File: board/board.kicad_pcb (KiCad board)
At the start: 2 copper layers, 21 x 29 mm, 12 parts, among them J1 004_BASE-T_CT_2x3, J2 013_PoE_rectified, Q1 TPN3300ANH,LQ, Q2 TPN3300ANH,LQ, Q3 TPN3300ANH,LQ, Q4 TPN3300ANH,LQ, Q5 TPN3300ANH,LQ, Q6 TPN3300ANH,LQ, Q7 TPN3300ANH,LQ, Q8 TPN3300ANH,LQ, U1 LT4321

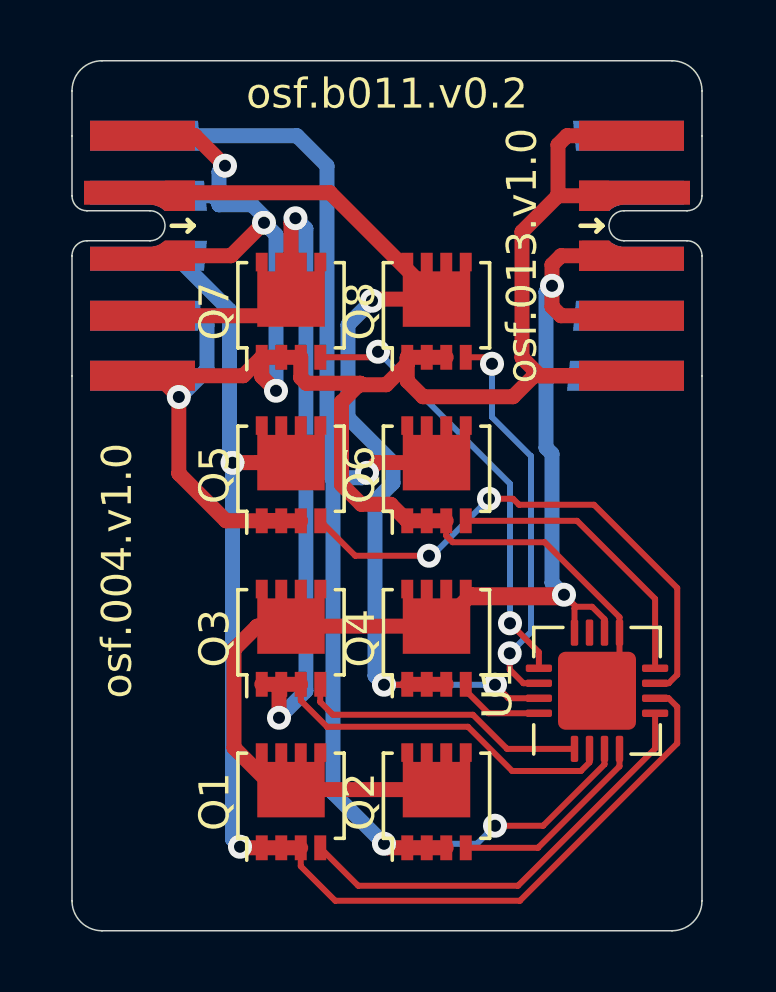
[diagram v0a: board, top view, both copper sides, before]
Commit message: updated connectors, changed mosfets and added enable resistors
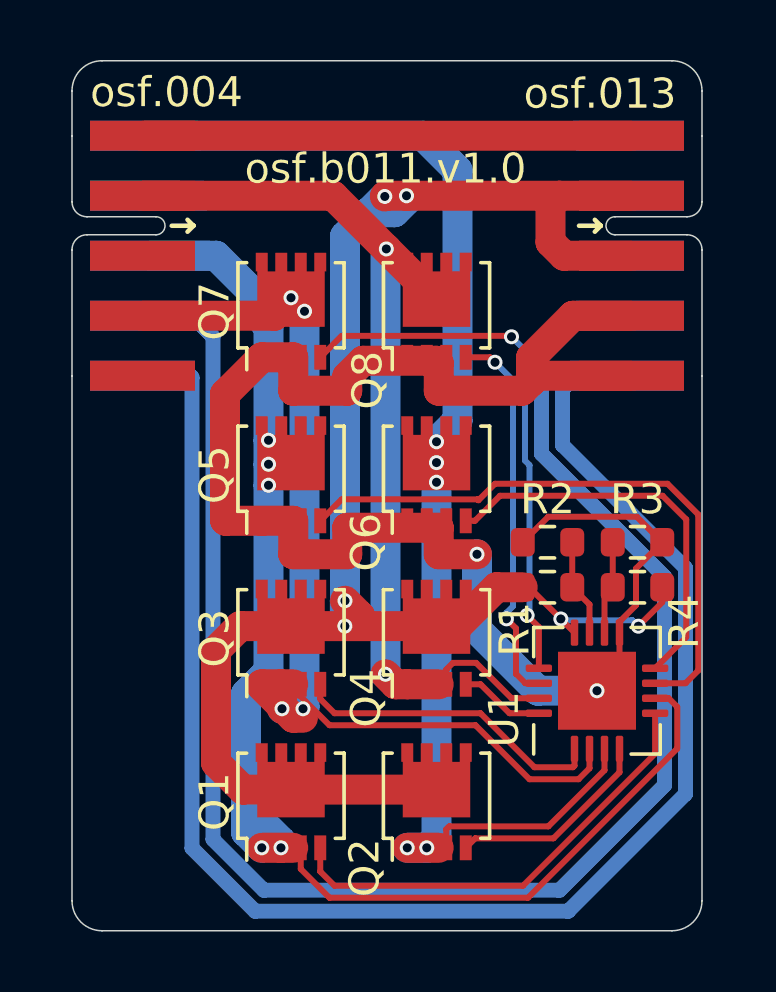
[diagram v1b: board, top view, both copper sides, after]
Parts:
- added R1: 0R, Resistor_SMD:R_0603_1608Metric, F.Cu at (135.8, 97.5)
- added R2: d.n.p, Resistor_SMD:R_0603_1608Metric, F.Cu at (135.8, 96.0)
- added R3: 0R, Resistor_SMD:R_0603_1608Metric, F.Cu at (138.8, 96.0)
- added R4: d.n.p, Resistor_SMD:R_0603_1608Metric, F.Cu at (138.8, 97.5)
- Q1, Q2, Q3, Q4, Q5, Q6, Q7, Q8: value TPN3300ANH,LQ -> PSMN075-100MSEX
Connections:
- J1 pad 10: GND -> Net-(J1-Pad10)
- J1 pad 3: GND -> (no net)
- J1 pad 5: GND -> (no net)
- J1 pad 7: GND -> (no net)
- J1 pad 9: GND -> Net-(J1-Pad9)
- J2 pad 10: (no net) -> Net-(J1-Pad10)
- J2 pad 2: GND -> /snippet/VPORTP
- J2 pad 4: /snippet/VPORTP -> /snippet/VPORTN
- J2 pad 5: GND -> /snippet/VPORTN
- J2 pad 9: (no net) -> Net-(J1-Pad9)
- Q5 pad 1: GND -> /snippet/VPORTN
- Q5 pad 2: GND -> /snippet/VPORTN
- Q5 pad 3: GND -> /snippet/VPORTN
- Q6 pad 1: GND -> /snippet/VPORTN
- Q6 pad 2: GND -> /snippet/VPORTN
- Q6 pad 3: GND -> /snippet/VPORTN
- Q7 pad 1: GND -> /snippet/VPORTN
- Q7 pad 2: GND -> /snippet/VPORTN
- Q7 pad 3: GND -> /snippet/VPORTN
- Q8 pad 1: GND -> /snippet/VPORTN
- Q8 pad 2: GND -> /snippet/VPORTN
- Q8 pad 3: GND -> /snippet/VPORTN
- U1 pad 10: /snippet/VPORTP -> /snippet/~{EN}
- U1 pad 11: /snippet/PWRGD -> /snippet/EN
- U1 pad 17: GND -> /snippet/VPORTN
- U1 pad 9: GND -> /snippet/VPORTN
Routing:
- net GND: track 90.0 -> 16.3 mm, vias 4 -> 0
- net Net-(J1-Pad9): track 0.00 -> 56.3 mm
- net /snippet/VPORTN: track 0.00 -> 55.8 mm, vias 0 -> 2
- net Net-(J1-Pad10): track 0.00 -> 53.9 mm
- net /snippet/VPORTP: track 46.2 -> 59.5 mm, vias 2 -> 6
- net /snippet/CT_36: track 42.9 -> 35.6 mm, vias 2 -> 4
- net /snippet/BG_45: track 9.70 -> 13.4 mm
- net /snippet/BG_36: track 14.8 -> 18.2 mm
- net /snippet/EN: track 0.00 -> 3.25 mm
- net /snippet/~{EN}: track 0.00 -> 3.13 mm
- net /snippet/CT_12: track 33.8 -> 31.5 mm, vias 3 -> 2
- net /snippet/BG_78: track 18.1 -> 20.4 mm, vias 2 -> 0
- net /snippet/CT_45: track 44.7 -> 43.1 mm, vias 3 -> 5
- net /snippet/CT_78: track 44.9 -> 44.0 mm, vias 2 -> 5
- net /snippet/TG_36: track 9.71 -> 10.5 mm
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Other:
- board text added: "osf.004"
- board text added: "osf.013"
- board text added: "osf.b011.v1.0"
- board text removed: "osf.004.v1.0"
- board text removed: "osf.013.v1.0"
- board text removed: "osf.b011.v0.2"

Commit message: added enable input from downstream
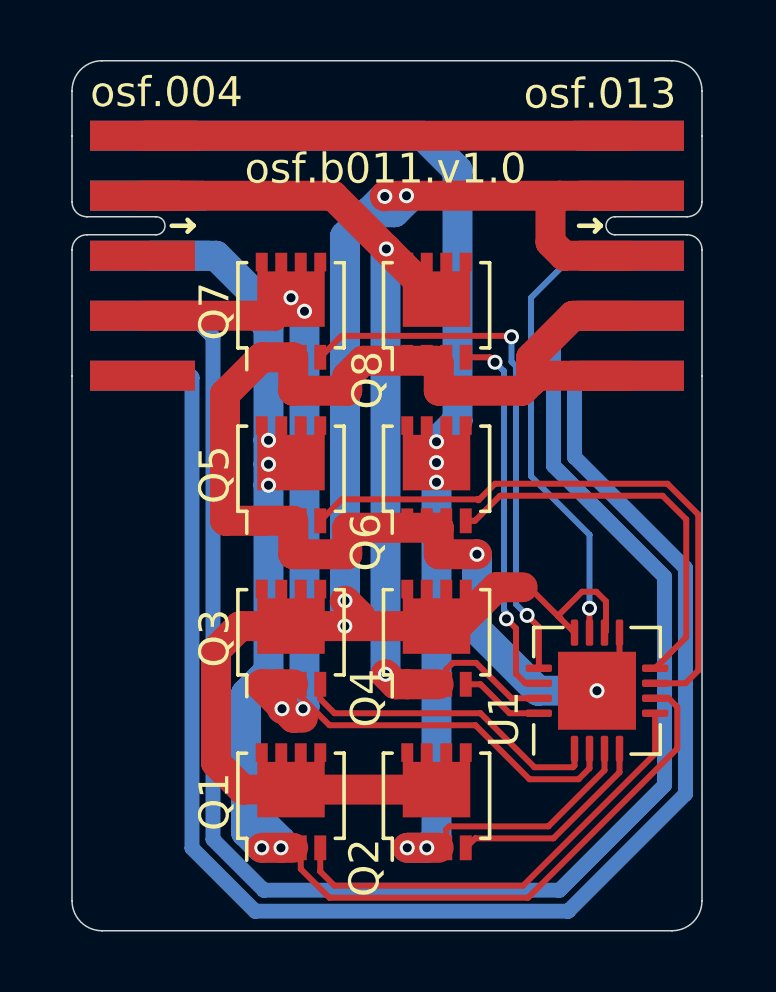
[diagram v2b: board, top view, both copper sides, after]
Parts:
- removed R1, R3: 0R, Resistor_SMD:R_0603_1608Metric
- removed R2, R4: d.n.p, Resistor_SMD:R_0603_1608Metric
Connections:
- J2 pad 8: (no net) -> /snippet/EN
- U1 pad 10: /snippet/~{EN} -> /snippet/VPORTP
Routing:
- net /snippet/EN: track 3.25 -> 15.9 mm, vias 0 -> 1
- net /snippet/VPORTN: track 55.8 -> 46.9 mm
- net /snippet/~{EN}: track 3.13 -> 0.00 mm
- net /snippet/VPORTP: track 59.5 -> 58.3 mm, vias 6 -> 4
